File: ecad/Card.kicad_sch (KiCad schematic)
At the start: 61 parts, among them J1 Conn_01x03_Pin, J2 USB_C_Receptacle_USB2.0_14P, SW14 SW_Push, SW15 SW_Push, U3 RP2350_80QFN, U4 W25Q128JVS, U5 MCP23017_SO, U6 MCP23017_SO, U7 NCP1117-3.3_SOT223, X1 ABM8-272-T3

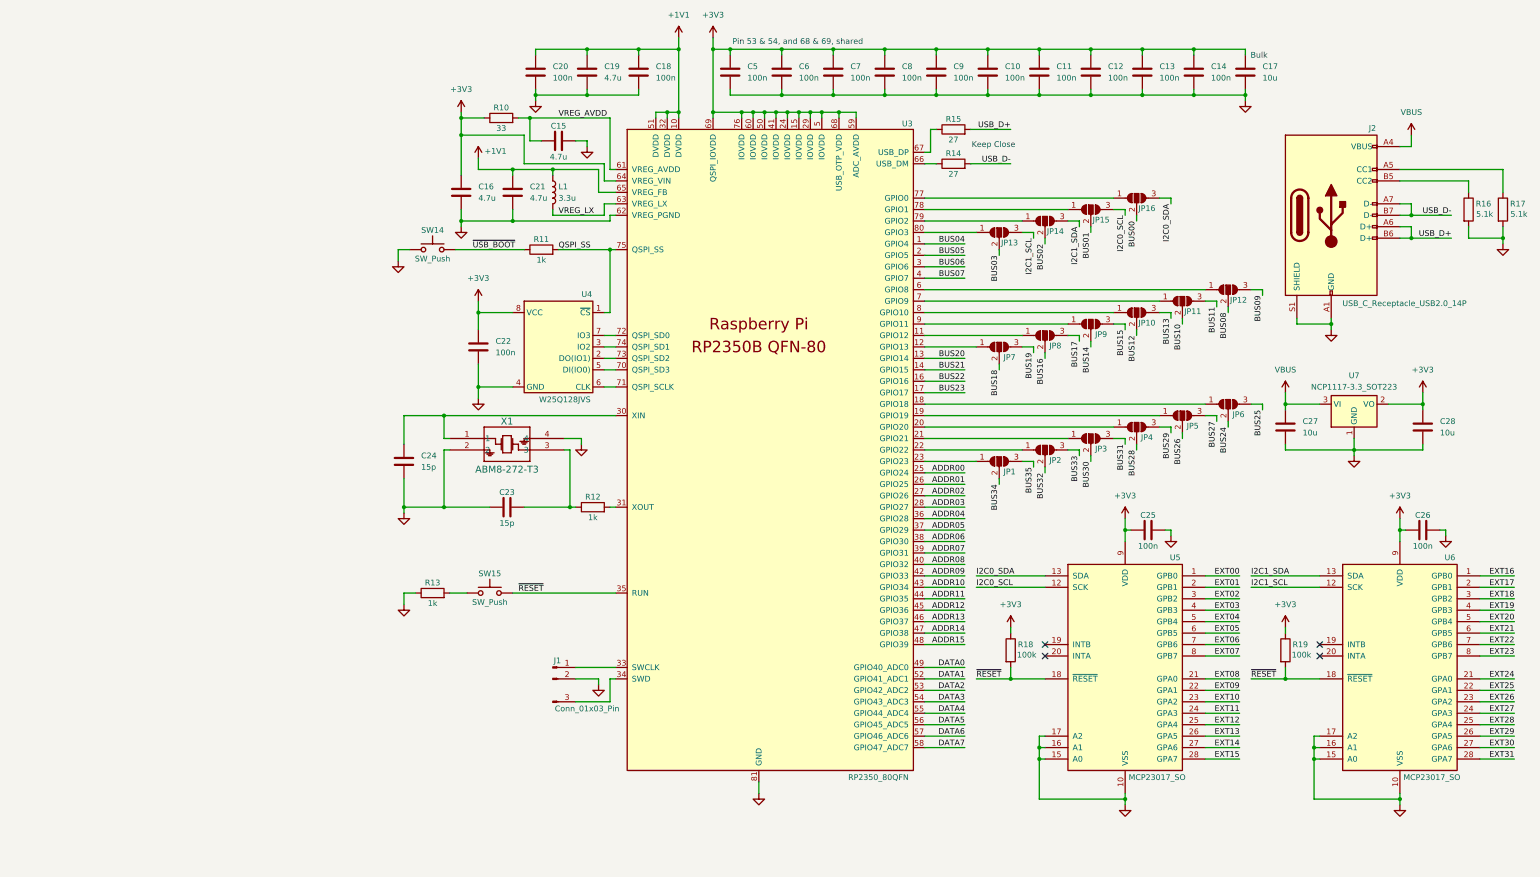
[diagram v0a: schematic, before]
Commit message: lib additions
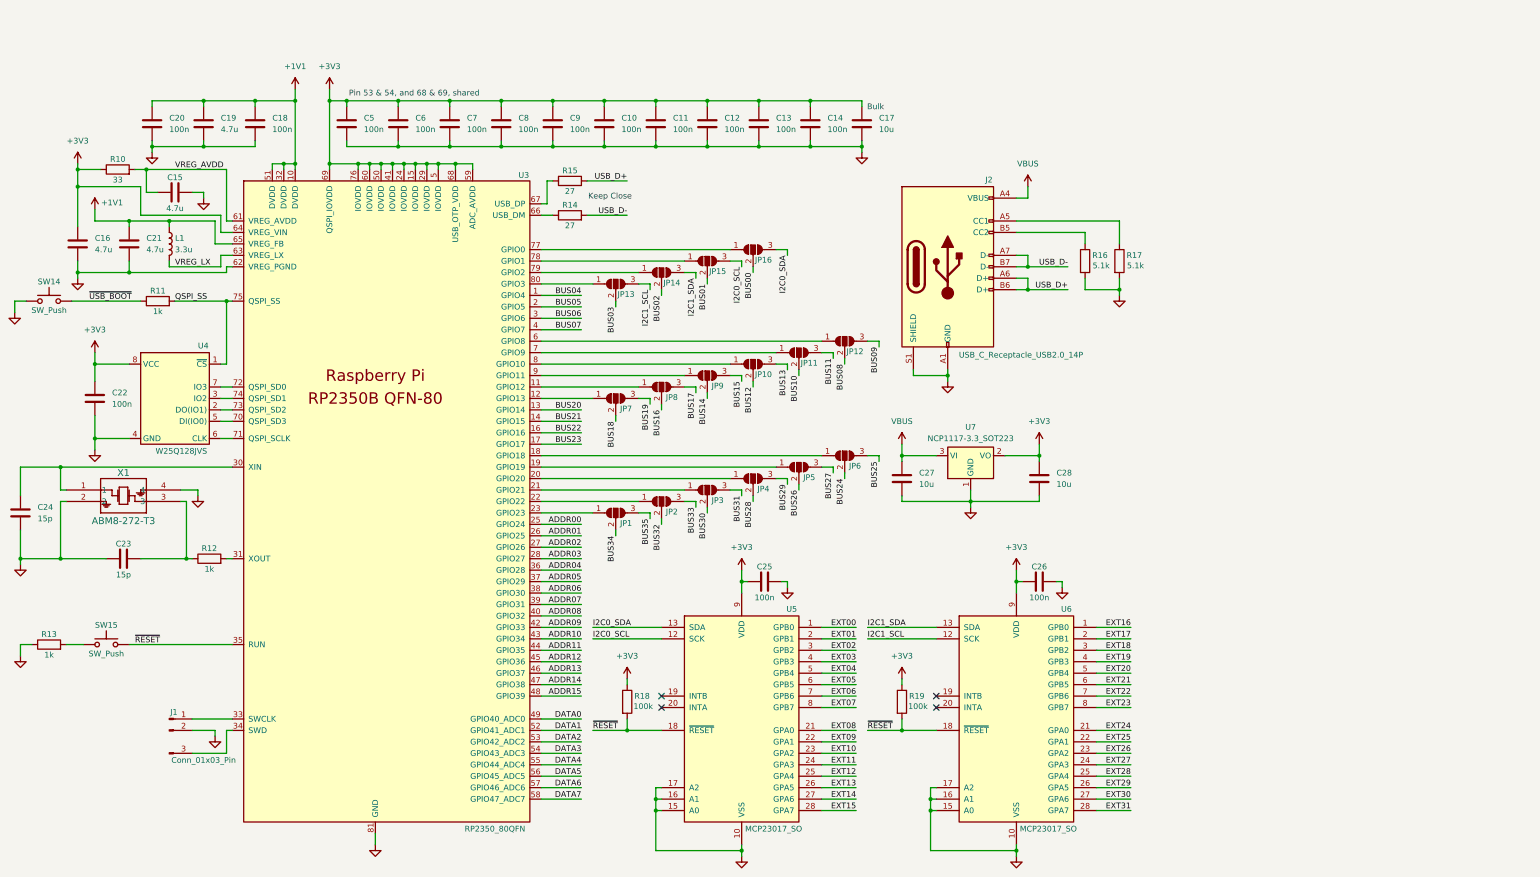
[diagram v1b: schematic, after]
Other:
- moved on the sheet: C10, C11, C12, C13, C14, C15, C16, C17, C18, C19, C20, C21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
